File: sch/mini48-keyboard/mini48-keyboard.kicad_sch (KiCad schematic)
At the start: 1 part

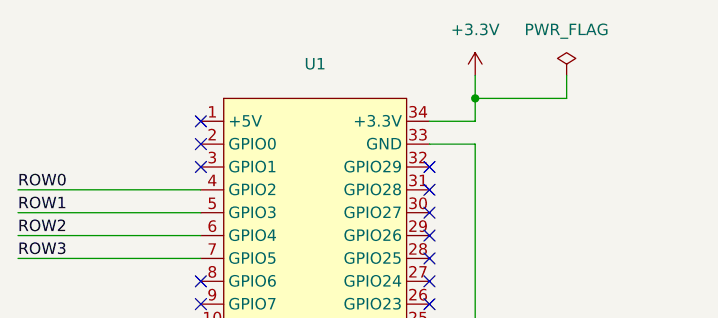
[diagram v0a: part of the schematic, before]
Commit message: 外形の微調整を行いました。 GNDベタにビアを打ちました。 余分なキーを切り離せるように、基板にスリットをいれました。
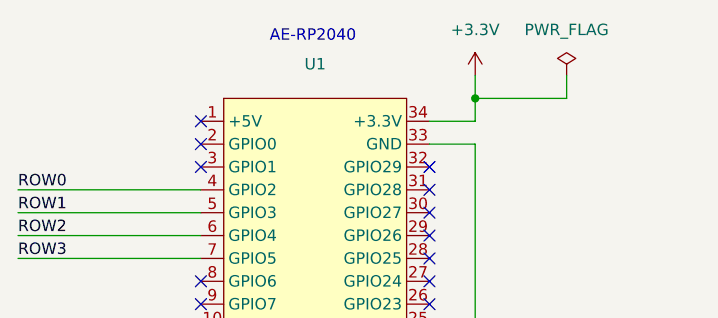
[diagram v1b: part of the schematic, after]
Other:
- note added: "AE-RP2040"
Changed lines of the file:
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@@
+		)
+	)
+	(text "AE-RP2040"
+		(exclude_from_sim no)
+		(at 51.816 33.782 0)
+		(effects
+			(font
+				(size 1.27 1.27)
+			)
 		)
 	)
